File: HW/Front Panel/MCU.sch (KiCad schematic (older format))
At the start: 37 parts, among them J1 CTRL, J2 MODE, J3 I2C, J4 ICE, J5 CAL, J6 PWM_DUAL, J7 CTRL_IN, J8 SERIAL, U1 KB817, U2 M0516LDN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

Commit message: Front Panel MCU pins reorganized
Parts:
- removed R12, R13: R, Resistors_SMD:R_1206_HandSoldering, symbol R
- removed R15, R16: R, Resistors_SMD:R_0603_HandSoldering, symbol R
- removed U1, U4: KB817, Opto-Devices:Optocoupler_SMD_HandSoldering_KPC357_LTV35x_PC357_SingleChannel, symbol KB817
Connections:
- net labels added: PP0, PP1, PP2, PP3, PP4, PP5, PP6, PP7, PWM_2, PWM_3, SPI_MISO, SPI_MOSI, SPI_SCK, SPI_SS
- wire segments 157 -> 159
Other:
- moved on the sheet: J7
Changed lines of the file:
@@
 LIBS:contrib
 LIBS:valves
-LIBS:MCU-cache
+LIBS:suf_led
 EELAYER 25 0
 EELAYER END
@@
 Wire Wire Line
 	8425 1250 8425 2550
-Text GLabel 4100 1775 1    40   Input ~ 0
+Text GLabel 3800 1775 1    40   Input ~ 0
 ADC_I
-Text GLabel 4200 1775 1    40   Input ~ 0
+Text GLabel 3700 1775 1    40   Input ~ 0
 ADC_U
 Text GLabel 4300 1775 1    40   Input ~ 0
@@
 	-1   0    0    -1
 $EndComp
-Text GLabel 4975 2450 2    40   Input ~ 0
+Text GLabel 3300 1775 1    40   Input ~ 0
 MODE_RPM
-Text GLabel 4975 2550 2    40   Input ~ 0
+Text GLabel 2700 3450 0    40   Input ~ 0
 MODE_AUTO
-Text GLabel 4975 2650 2    40   Input ~ 0
+Text GLabel 4300 4000 3    40   Input ~ 0
 CAL
 Text GLabel 8375 1550 0    40   Input ~ 0
 TFT_DC
-Text GLabel 3800 1775 1    40   Input ~ 0
+Text GLabel 3900 4000 3    40   Input ~ 0
 TFT_DC
 Wire Wire Line
@@
 Text GLabel 8375 1450 0    40   Input ~ 0
 TFT_RST
-Text GLabel 3700 1775 1    40   Input ~ 0
+Text GLabel 4000 4000 3    40   Input ~ 0
 TFT_RST
-Text GLabel 3600 1775 1    40   Input ~ 0
+Text GLabel 4200 1775 1    40   Input ~ 0
 RXD
 Text GLabel 5950 6775 2    40   Input ~ 0
 RXD
-Text GLabel 3500 1775 1    40   Input ~ 0
+Text GLabel 4100 1775 1    40   Input ~ 0
 TXD
 Text GLabel 5950 6875 2    40   Input ~ 0
@@
 Text GLabel 8375 1350 0    40   Input ~ 0
 TFT_CS
-Text GLabel 3400 1775 1    40   Input ~ 0
+Text GLabel 4975 2450 2    40   Input ~ 0
 TFT_CS
 Text GLabel 8375 1650 0    40   Input ~ 0
 TFT_MOSI
-Text GLabel 2725 2350 0    40   Input ~ 0
+Text GLabel 4975 2550 2    40   Input ~ 0
 TFT_MOSI
-Text GLabel 2725 2450 0    40   Input ~ 0
+Text GLabel 4975 2650 2    40   Input ~ 0
 TFT_MISO
-Text GLabel 2725 2550 0    40   Input ~ 0
+Text GLabel 4975 2750 2    40   Input ~ 0
 TFT_SCK
 Text GLabel 8375 1950 0    40   Input ~ 0
@@
 Wire Wire Line
 	2850 2550 2725 2550
-Text GLabel 3900 4000 3    40   Input ~ 0
+Text GLabel 4975 3350 2    40   Input ~ 0
 PWM_0
-Text GLabel 4000 4000 3    40   Input ~ 0
+Text GLabel 4975 3250 2    40   Input ~ 0
 PWM_1
 Text GLabel 4400 4000 3    40   Input ~ 0
@@
 	4000 950  4000 1900
 $Comp
-L CONN_4 J7
-U 1 1 557F42B8
-P 675 6750
-F 0 "J7" V 625 6750 40  0000 C CNN
-F 1 "CTRL_IN" V 725 6750 40  0000 C CNN
-F 2 "suf_connector_ncw:CONN_NCW254-04S" H 675 6750 60  0001 C CNN
-F 3 "" H 675 6750 60  0000 C CNN
-	1    675  6750
-	-1   0    0    -1
-$EndComp
-$Comp
 L GND #PWR015
 U 1 1 557F443A
-P 2275 7500
-F 0 "#PWR015" H 2275 7250 50  0001 C CNN
-F 1 "GND" H 2275 7350 50  0000 C CNN
-F 2 "" H 2275 7500 60  0000 C CNN
-F 3 "" H 2275 7500 60  0000 C CNN
-	1    2275 7500
+P 1075 7000
+F 0 "#PWR015" H 1075 6750 50  0001 C CNN
+F 1 "GND" H 1075 6850 50  0000 C CNN
+F 2 "" H 1075 7000 60  0000 C CNN
+F 3 "" H 1075 7000 60  0000 C CNN
+	1    1075 7000
 	1    0    0    -1
 $EndComp
@@
 P 3675 1275
 F 0 "#PWR026" H 3675 1025 50  0001 C CNN
-F 1 "GNDA" H 3675 1125 50  0000 C CNN
+F 1 "GNDA" H 3775 1150 50  0000 C CNN
 F 2 "" H 3675 1275 60  0000 C CNN
 F 3 "" H 3675 1275 60  0000 C CNN
@@
 L GNDA #PWR027
 U 1 1 55828EA4
-P 2675 2900
-F 0 "#PWR027" H 2675 2650 50  0001 C CNN
-F 1 "GNDA" H 2675 2750 50  0000 C CNN
-F 2 "" H 2675 2900 60  0000 C CNN
-F 3 "" H 2675 2900 60  0000 C CNN
-	1    2675 2900
-	1    0    0    -1
-$EndComp
-Wire Wire Line
-	2850 2850 2675 2850
-Wire Wire Line
-	2675 2850 2675 2900
+P 2325 2900
+F 0 "#PWR027" H 2325 2650 50  0001 C CNN
+F 1 "GNDA" H 2325 2750 50  0000 C CNN
+F 2 "" H 2325 2900 60  0000 C CNN
+F 3 "" H 2325 2900 60  0000 C CNN
+	1    2325 2900
+	1    0    0    -1
+$EndComp
+Wire Wire Line
+	2850 2850 2325 2850
+Wire Wire Line
+	2325 2850 2325 2900
 Wire Notes Line
 	7700 600  5875 600
@@
 Wire Wire Line
 	3600 3900 3600 4000
-$Comp
-L KB817 U4
-U 1 1 5582C384
-P 1825 6900
-F 0 "U4" H 1625 7100 50  0000 L CNN
-F 1 "KB817" H 1825 7100 50  0000 L CNN
-F 2 "Opto-Devices:Optocoupler_SMD_HandSoldering_KPC357_LTV35x_PC357_SingleChannel" H 1625 6700 50  0001 L CIN
-F 3 "" H 1825 6900 50  0000 L CNN
-	1    1825 6900
-	1    0    0    -1
-$EndComp
-$Comp
-L KB817 U1
-U 1 1 5582C401
-P 1825 6550
-F 0 "U1" H 1625 6750 50  0000 L CNN
-F 1 "KB817" H 1825 6750 50  0000 L CNN
-F 2 "Opto-Devices:Optocoupler_SMD_HandSoldering_KPC357_LTV35x_PC357_SingleChannel" H 1625 6350 50  0001 L CIN
-F 3 "" H 1825 6550 50  0000 L CNN
-	1    1825 6550
-	1    0    0    -1
-$EndComp
-$Comp
-L R R12
-U 1 1 5582CD5F
-P 1275 6450
-F 0 "R12" H 1275 6375 40  0000 C CNN
-F 1 "R" H 1275 6525 40  0000 C CNN
-F 2 "Resistors_SMD:R_1206_HandSoldering" H 1275 6450 60  0001 C CNN
-F 3 "" H 1275 6450 60  0000 C CNN
-	1    1275 6450
-	1    0    0    -1
-$EndComp
-$Comp
-L R R13
-U 1 1 5582CDE8
-P 1275 6800
-F 0 "R13" H 1275 6725 40  0000 C CNN
-F 1 "R" H 1275 6875 40  0000 C CNN
-F 2 "Resistors_SMD:R_1206_HandSoldering" H 1275 6800 60  0001 C CNN
-F 3 "" H 1275 6800 60  0000 C CNN
-	1    1275 6800
-	1    0    0    -1
-$EndComp
-Wire Wire Line
-	1025 6800 1075 6800
-Wire Wire Line
-	1475 6800 1525 6800
-Wire Wire Line
-	1025 6900 1025 7000
-Wire Wire Line
-	1025 7000 1525 7000
-Wire Wire Line
-	1025 6700 1525 6700
-Wire Wire Line
-	1525 6700 1525 6650
-Wire Wire Line
-	1525 6450 1475 6450
-Wire Wire Line
-	1075 6450 1025 6450
-Wire Wire Line
-	1025 6450 1025 6600
-$Comp
-L R R15
-U 1 1 5582D765
-P 2175 7250
-F 0 "R15" H 2175 7175 40  0000 C CNN
-F 1 "R" H 2175 7325 40  0000 C CNN
-F 2 "Resistors_SMD:R_0603_HandSoldering" H 2175 7250 60  0001 C CNN
-F 3 "" H 2175 7250 60  0000 C CNN
-	1    2175 7250
-	0    1    1    0
-$EndComp
-$Comp
-L R R16
-U 1 1 5582D84A
-P 2375 7250
-F 0 "R16" H 2375 7175 40  0000 C CNN
-F 1 "R" H 2375 7325 40  0000 C CNN
-F 2 "Resistors_SMD:R_0603_HandSoldering" H 2375 7250 60  0001 C CNN
-F 3 "" H 2375 7250 60  0000 C CNN
-	1    2375 7250
-	0    1    1    0
-$EndComp
-Wire Wire Line
-	2125 7000 2525 7000
-Wire Wire Line
-	2125 6650 2525 6650
-$Comp
-L VCC #PWR029
-U 1 1 5582DB47
-P 2175 6400
-F 0 "#PWR029" H 2175 6250 50  0001 C CNN
-F 1 "VCC" H 2175 6550 50  0000 C CNN
-F 2 "" H 2175 6400 60  0000 C CNN
-F 3 "" H 2175 6400 60  0000 C CNN
-	1    2175 6400
-	1    0    0    -1
-$EndComp
-Wire Wire Line
-	2175 6400 2175 6800
-Wire Wire Line
-	2175 6450 2125 6450
-Wire Wire Line
-	2175 6800 2125 6800
-Connection ~ 2175 6450
-Wire Wire Line
-	2175 7050 2175 7000
-Connection ~ 2175 7000
-Wire Wire Line
-	2375 7050 2375 6650
-Connection ~ 2375 6650
-Wire Wire Line
-	2175 7450 2375 7450
-Wire Wire Line
-	2275 7450 2275 7500
-Connection ~ 2275 7450
-Text GLabel 2525 6650 2    40   Input ~ 0
+Text GLabel 1125 6700 2    40   Input ~ 0
 SPINDLE_SPEED
-Text GLabel 2525 7000 2    40   Input ~ 0
+Text GLabel 1125 6800 2    40   Input ~ 0
 SPINDLE_SWITCH
-Text GLabel 4100 4000 3    40   Input ~ 0
+Text GLabel 3600 1775 1    40   Input ~ 0
 SPINDLE_SPEED
-Text GLabel 4200 4000 3    40   Input ~ 0
+Text GLabel 4975 3450 2    40   Input ~ 0
 SPINDLE_SWITCH
 Wire Wire Line
 	4200 3900 4200 4000
-Wire Notes Line
-	3125 6125 525  6125
-Wire Notes Line
-	525  6125 525  7725
-Wire Notes Line
-	525  7725 3125 7725
-Wire Notes Line
-	3125 7725 3125 6125
 Text Notes 1250 6225 2    60   ~ 0
 Spindle Control
@@
 Text Notes 5300 6225 0    60   ~ 0
 Serial
+Wire Wire Line
+	4975 2750 4850 2750
+Wire Wire Line
+	4300 3900 4300 4000
+Wire Wire Line
+	4975 3250 4850 3250
+Wire Wire Line
+	4975 3350 4850 3350
+Text GLabel 4975 2350 2    40   Input ~ 0
+SPINDLE_SPEED
+Wire Wire Line
+	4975 2350 4850 2350
+Wire Wire Line
+	3300 1775 3300 1900
+Wire Wire Line
+	2850 3450 2700 3450
+Text GLabel 3400 1775 1    40   Input ~ 0
+SPI_SS
+Text GLabel 2725 2350 0    40   Input ~ 0
+SPI_MOSI
+Text GLabel 2725 2450 0    40   Input ~ 0
+SPI_MISO
+Text GLabel 2725 2550 0    40   Input ~ 0
+SPI_SCK
+Wire Wire Line
+	4975 3450 4850 3450
+Text GLabel 4100 4000 3    40   Input ~ 0
+PWM_2
+Text GLabel 4200 4000 3    40   Input ~ 0
+PWM_3
+Text GLabel 2725 2750 0    40   Input ~ 0
+PP0
+Text GLabel 2725 2950 0    40   Input ~ 0
+PP1
+Text GLabel 2725 3050 0    40   Input ~ 0
+PP2
+Text GLabel 2725 3150 0    40   Input ~ 0
+PP3
+Text GLabel 2725 3250 0    40   Input ~ 0
+PP4
+Text GLabel 2725 3350 0    40   Input ~ 0
+PP5
+Text GLabel 3300 4000 3    40   Input ~ 0
+PP6
+Text GLabel 3400 4000 3    40   Input ~ 0
+PP7
+Wire Wire Line
+	3400 3900 3400 4000
+Wire Wire Line
+	3300 3900 3300 4000
+Wire Wire Line
+	2850 3350 2725 3350
+Wire Wire Line
+	2850 3250 2725 3250
+Wire Wire Line
+	2850 3150 2725 3150
+Wire Wire Line
+	2850 3050 2725 3050
+Wire Wire Line
+	2850 2750 2725 2750
+Wire Wire Line
+	2850 2950 2725 2950
+$Comp
+L VCC #PWR029
+U 1 1 5582DB47
+P 1075 6450
+F 0 "#PWR029" H 1075 6300 50  0001 C CNN
+F 1 "VCC" H 1075 6600 50  0000 C CNN
+F 2 "" H 1075 6450 60  0000 C CNN
+F 3 "" H 1075 6450 60  0000 C CNN
+	1    1075 6450
+	1    0    0    -1
+$EndComp
+Wire Wire Line
+	1075 6800 1125 6800
+Wire Wire Line
+	1075 6450 1075 6600
+Wire Wire Line
+	1075 6900 1075 7000
+$Comp
+L CONN_4 J7
+U 1 1 557F42B8
+P 725 6750
+F 0 "J7" V 675 6750 40  0000 C CNN
+F 1 "CTRL_IN" V 775 6750 40  0000 C CNN
+F 2 "suf_connector_ncw:CONN_NCW254-04S" H 725 6750 60  0001 C CNN
+F 3 "" H 725 6750 60  0000 C CNN
+	1    725  6750
+	-1   0    0    -1
+$EndComp
+Wire Wire Line
+	1125 6700 1075 6700
+Wire Notes Line
+	525  6125 1750 6125
+Wire Notes Line
+	1750 6125 1750 7200
+Wire Notes Line
+	1750 7200 525  7200
+Wire Notes Line
+	525  7200 525  6125
 $EndSCHEMATC

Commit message: Before Front Panel next revision
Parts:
- added J10: SPI, Pin_Headers:Pin_Header_Straight_2x05, symbol CONN_5X2
- added J11: EXT_PWM, suf_connector_ncw:CONN_NCW254-03S, symbol CONN_3
- added J12: EXT_PWM_DUAL, Pin_Headers:Pin_Header_Straight_1x03, symbol CONN_3
- added J13: 1Wire, suf_connector_ncw:CONN_NCW254-03S, symbol CONN_3
- added J14, J15, J16, J17: JUMPER, Pin_Headers:Pin_Header_Straight_1x02, symbol JUMPER
- added J9: CTRL, Pin_Headers:Pin_Header_Straight_2x08, symbol CONN_8X2
- E1: footprint suf_switch:EC11P20_single_side -> suf_switch:EC11P20
- J4: footprint (none) -> Pin_Headers:Pin_Header_Straight_1x05
- J7: footprint suf_connector_ncw:CONN_NCW254-04S -> Pin_Headers:Pin_Header_Straight_1x04
- X1: footprint (none) -> Crystals:Crystal_HC49-SD_SMD
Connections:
- net GND: now also J10.9, J13.3 (P3), J9.1, J9.11, J9.13, J9.15, J9.3, J9.5, J9.7, J9.9
- net GNDA: now also J10.1, J10.3, J10.5, J10.7, J11.3 (P3)
- net PP0: now also J9.2
- net PP1: now also J9.4
- net PP2: now also J9.6
- net PP3: now also J9.8
- net PP4: now also J9.10
- net PP5: now also J9.12
- net PP6: now also J9.14
- net PP7: now also J9.16
- net PWM_0: now also J1.12
- net PWM_2: now also J11.1 (P1), J12.1 (P1)
- net PWM_3: now also J12.2 (PM)
- net SPI_MISO: now also J10.6, J16.2
- net SPI_MOSI: now also J10.4, J15.2
- net SPI_SCK: now also J10.8, J17.2
- net SPI_SS: now also J10.2, J14.2
- net VCC: now also J10.10, J13.1 (P1)
- net 1Wire: now reaches U2.46 (P1.3)
- net 1Wire: now also J13.2 (PM)
- net at U3.15 (SD_CS): now also J14.1
- net at U3.16 (SD_MOSI): now also J15.1
- net at U3.17 (SD_MISO): now also J16.1
- net at U3.18 (SD_SCK): now also J17.1
- net at J6.3 (P3): now also J1.14
- new net: J11.2 (PM), J12.3 (P3)
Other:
- note added: "1Wire / Analog In"
- note added: "Calibration Control"
- note added: "External Header\n(for future add-ons)"
- note added: "External PWM\n(for future add-ons)"
- note added: "I2C\n(for future add-ons)"
- note added: "Mode Control"
- note added: "SPI / Analog\n(for future add-ons)"
- note removed: "I2C"
- moved on the sheet: C1, C2, C6, C7, E1, J1, J2, J3, J5, J6, J7, J8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

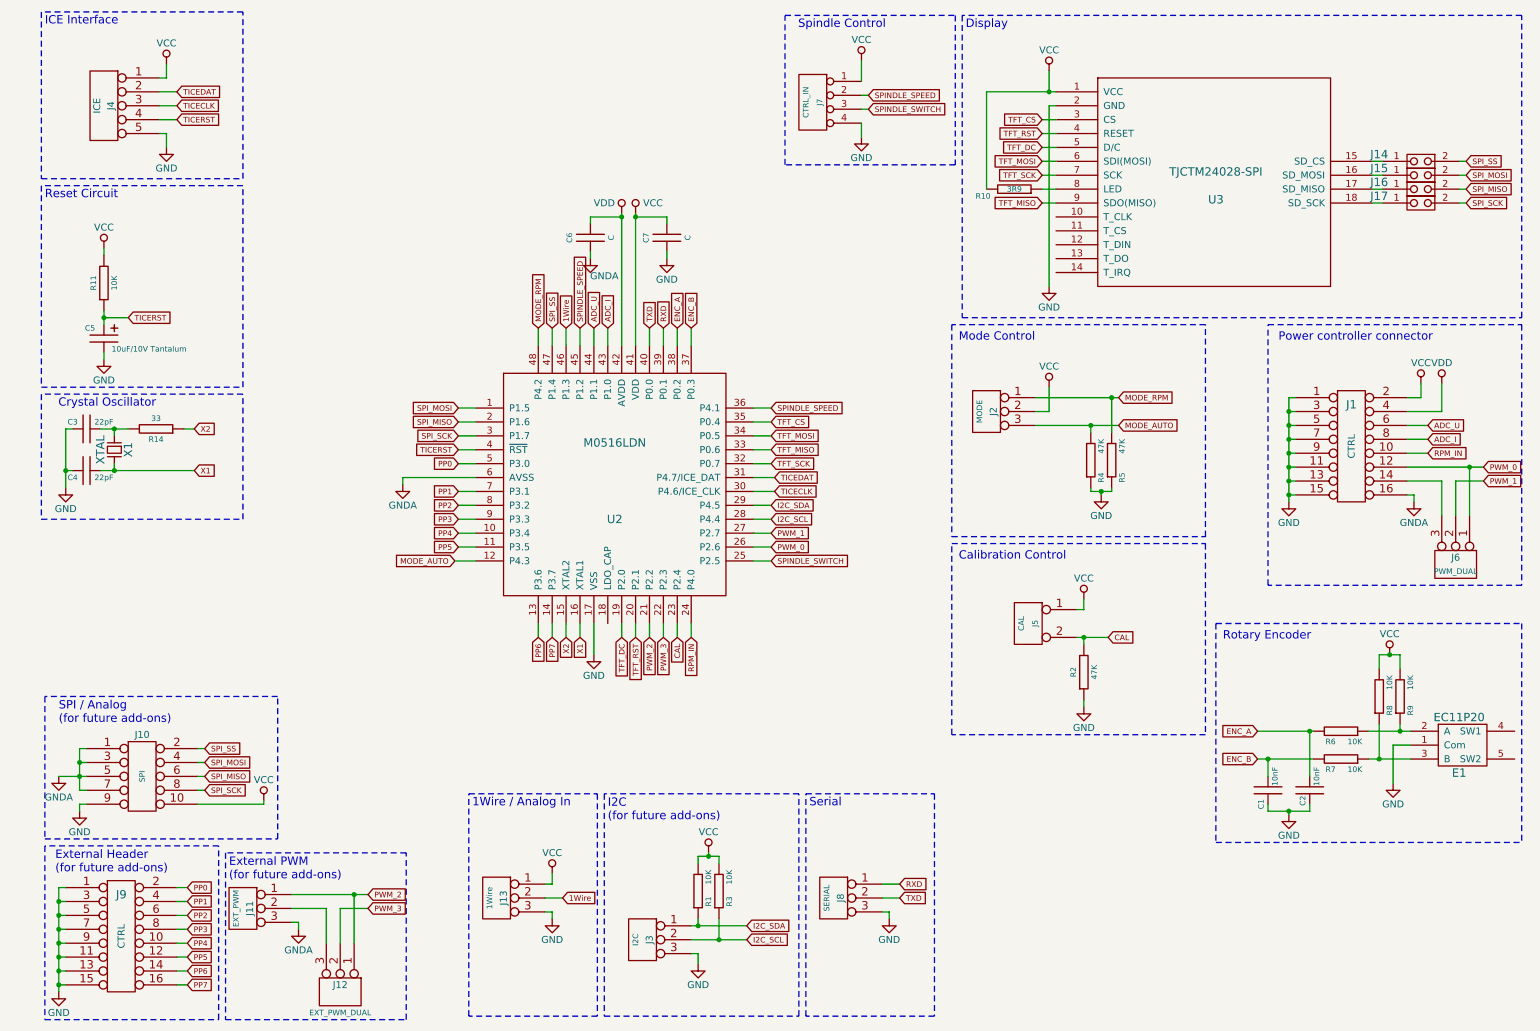
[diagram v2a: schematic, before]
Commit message: Front Panel schematic 1.01 added
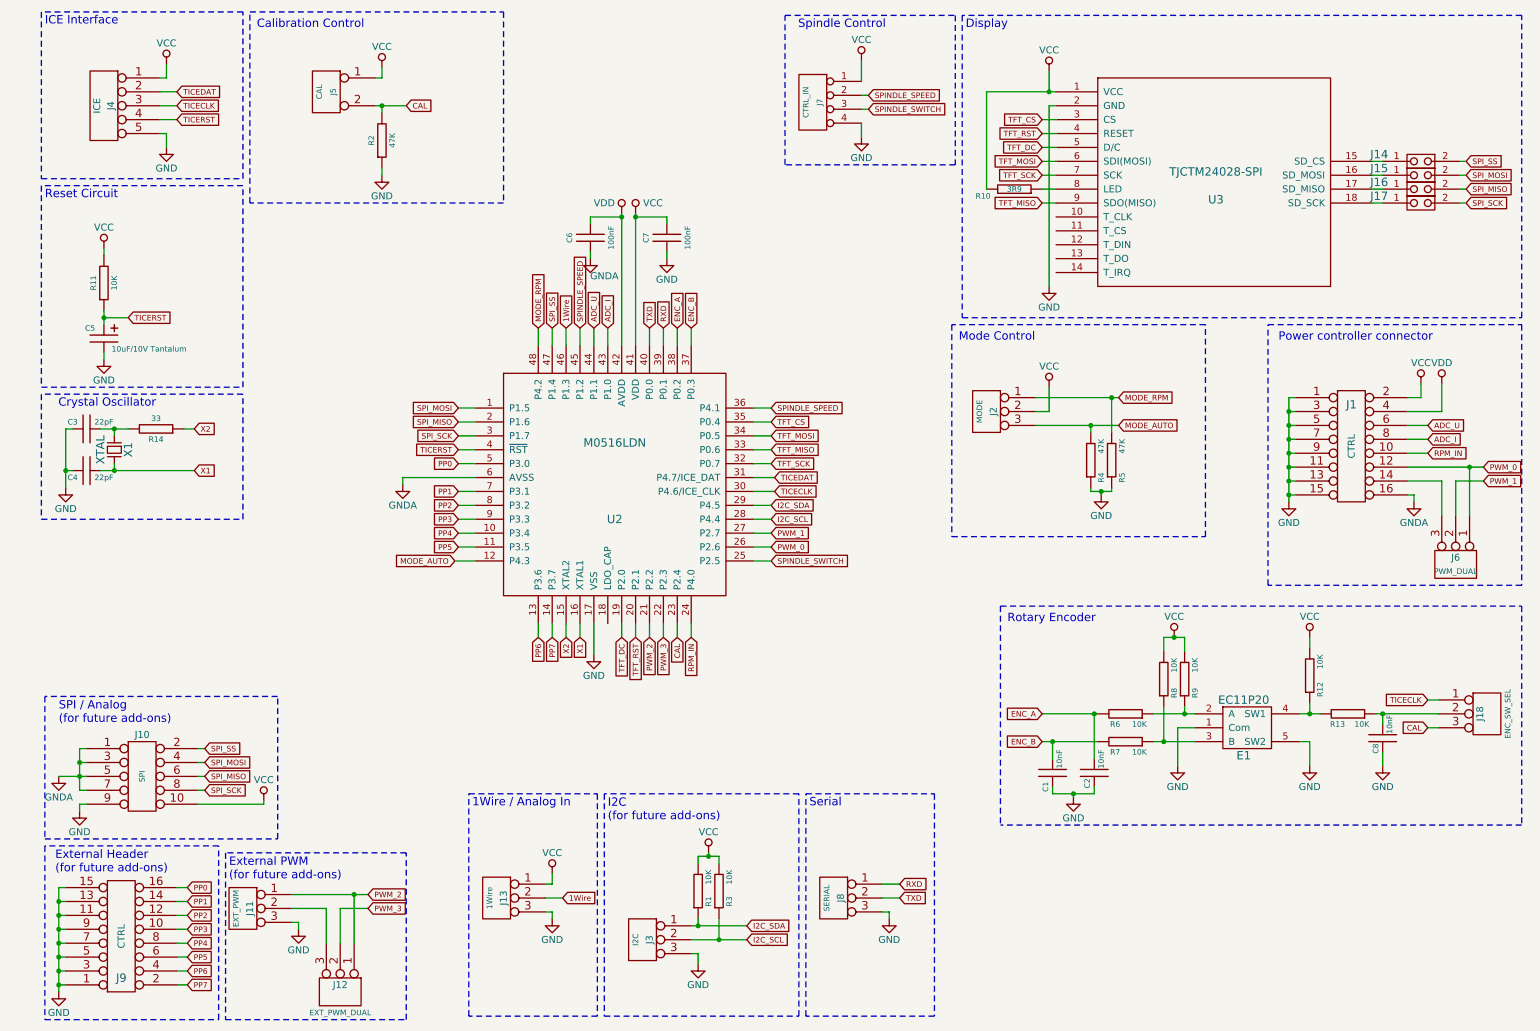
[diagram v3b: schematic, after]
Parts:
- added C8: 10nF, Capacitors_SMD:C_0603_HandSoldering, symbol C
- added J18: ENC_SW_SEL, Pin_Headers:Pin_Header_Straight_1x03, symbol CONN_3
- added R12, R13: 10K, Resistors_SMD:R_0603_HandSoldering, symbol R
- C6, C7: value C -> 100nF
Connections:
- net CAL: now also J18.3 (P3)
- net GND: now also E1.5 (SW2), J11.3 (P3), C8.2
- net GNDA: no longer J11.3 (P3)
- net PP0: now also J9.16; no longer J9.2
- net PP1: now also J9.14; no longer J9.4
- net PP2: now also J9.12; no longer J9.6
- net PP3: now also J9.10; no longer J9.8
- net PP4: now also J9.8; no longer J9.10
- net PP5: now also J9.6; no longer J9.12
- net PP6: now also J9.4; no longer J9.14
- net PP7: now also J9.2; no longer J9.16
- net TICECLK: now also J18.1 (P1)
- net VCC: now also R12.1
- net at E1.4 (SW1): now also R12.2, R13.1
- new net: C8.1, J18.2 (PM), R13.2
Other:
- moved on the sheet: C1, C2, E1, J5, R2, R6, R7, R8, R9

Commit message: Front Panel Schematic v1.01 + PCB design added
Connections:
- net PWM_1: now also J6.3 (P3); no longer J6.2 (PM)
- net PWM_3: now also J12.3 (P3); no longer J12.2 (PM)
- net at J1.14: now also J6.2 (PM); no longer J6.3 (P3)
- net at J11.2 (PM): now also J12.2 (PM); no longer J12.3 (P3)
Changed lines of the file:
@@
 $EndComp
-Wire Wire Line
-	10325 3875 10575 3875
-Wire Wire Line
-	10575 3875 10575 4125
 Wire Wire Line
 	10325 3775 10875 3775
@@
 Text GLabel 10875 3775 2    40   Input ~ 0
 PWM_0
-Text GLabel 10875 3875 2    40   Input ~ 0
+Text GLabel 10875 3950 2    40   Input ~ 0
 PWM_1
 Connection ~ 10775 3775
-Wire Wire Line
-	10675 3875 10875 3875
-Wire Wire Line
-	10675 3875 10675 4125
 Wire Wire Line
 	4675 4900 4675 5000
@@
 $EndComp
 Wire Wire Line
-	2300 6950 2550 6950
-Wire Wire Line
-	2550 6950 2550 7200
-Wire Wire Line
 	2300 6850 2850 6850
 Wire Wire Line
@@
 Text GLabel 2850 6850 2    40   Input ~ 0
 PWM_2
-Text GLabel 2850 6950 2    40   Input ~ 0
+Text GLabel 2850 7025 2    40   Input ~ 0
 PWM_3
 Connection ~ 2750 6850
-Wire Wire Line
-	2650 6950 2850 6950
-Wire Wire Line
-	2650 6950 2650 7200
 Wire Wire Line
 	2300 7050 2350 7050
@@
 	1    0    0    -1
 $EndComp
+Wire Wire Line
+	10325 3875 10675 3875
+Wire Wire Line
+	10675 3875 10675 4125
+Wire Wire Line
+	10875 3950 10575 3950
+Wire Wire Line
+	10575 3950 10575 4125
+Wire Wire Line
+	2850 7025 2550 7025
+Wire Wire Line
+	2550 7025 2550 7200
+Wire Wire Line
+	2300 6950 2650 6950
+Wire Wire Line
+	2650 6950 2650 7200
 $EndSCHEMATC
